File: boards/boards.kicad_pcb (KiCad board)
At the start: 2 copper layers, 34 parts, among them J1 MicroSD, P1 CONN_01X04, P10 , P11 , P12 , P13 CONN_01X02, P2 , P3 , P4 , P5 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

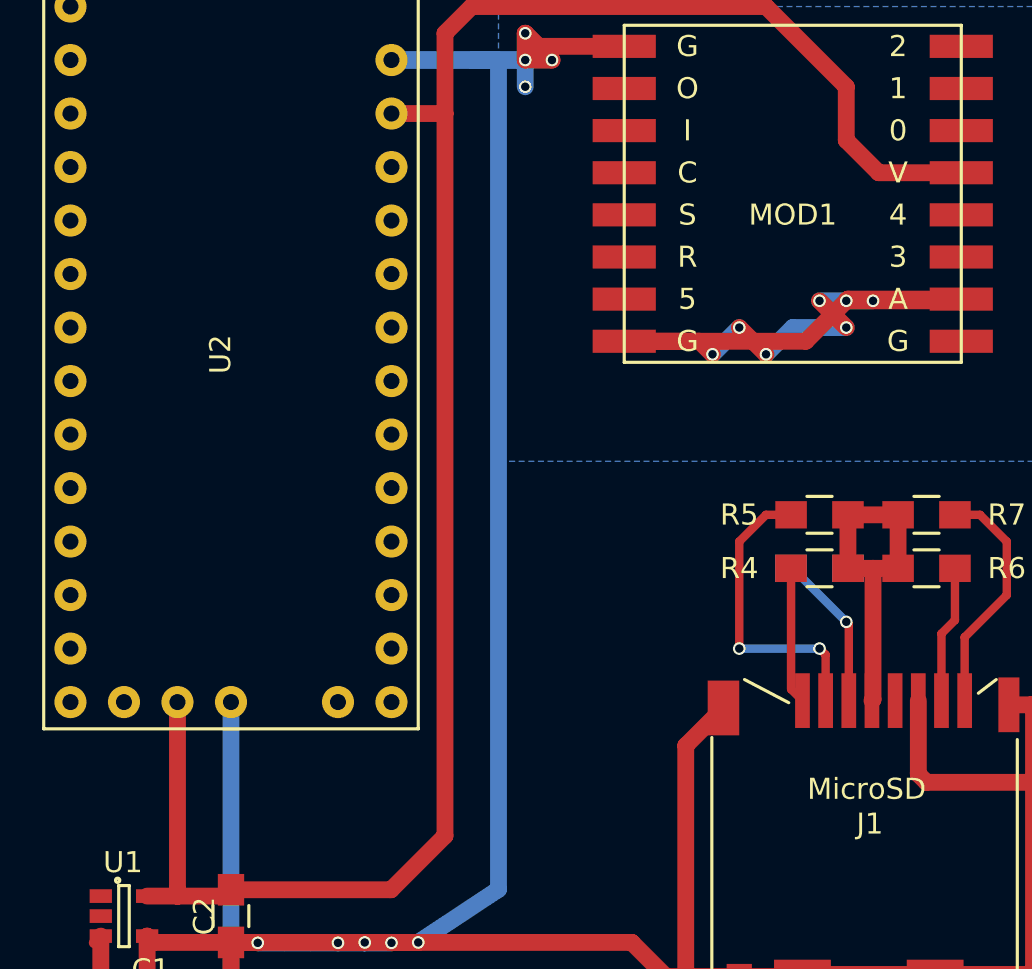
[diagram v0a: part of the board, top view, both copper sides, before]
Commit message: Continued routing SPI pins. Added some relevant offline docs.
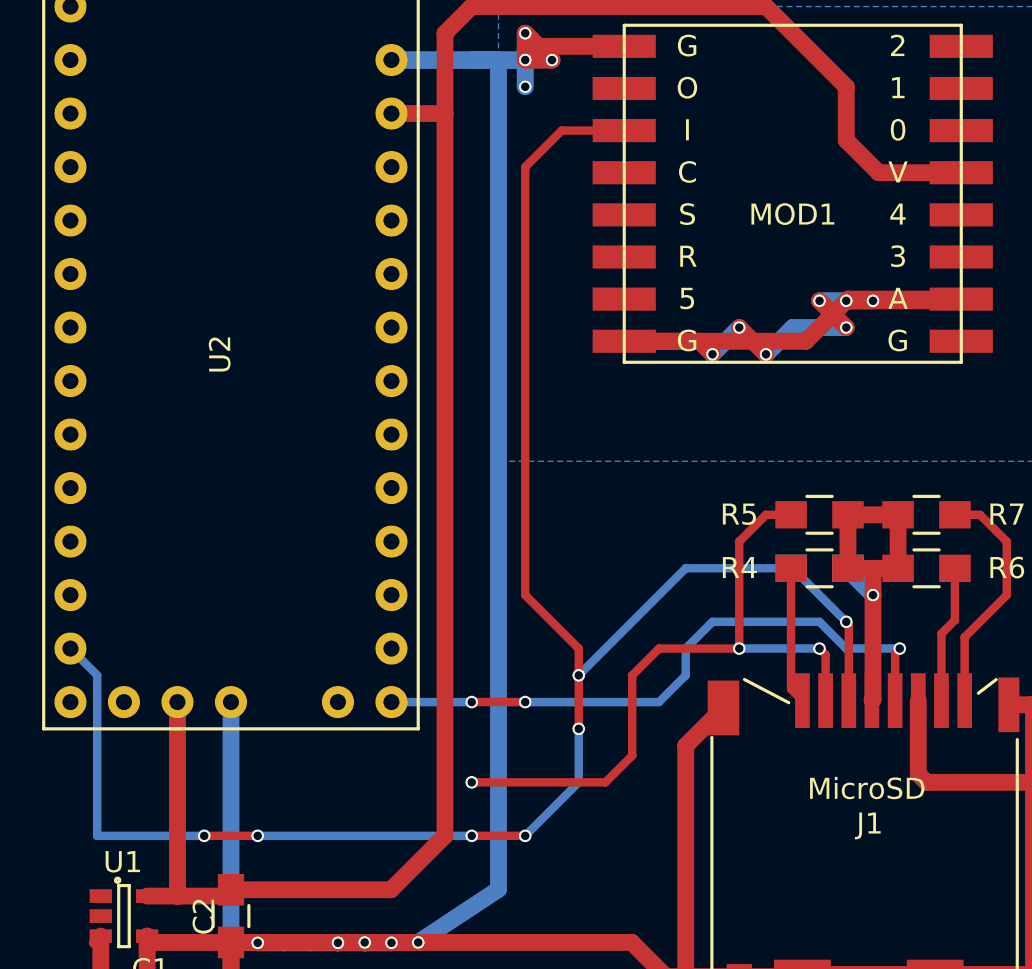
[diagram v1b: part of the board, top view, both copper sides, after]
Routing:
- net Net-(J1-Pad3): track 7.46 -> 88.7 mm, vias 1 -> 7
- net Net-(J1-Pad5): track 0.00 -> 29.5 mm, vias 0 -> 3
- net Net-(J1-Pad2): track 14.5 -> 32.0 mm, vias 2 -> 3
- net +3V3: track 112.2 -> 113.9 mm, vias 0 -> 1
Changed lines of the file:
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@@
   (general
     (links 77)
-    (no_connects 49)
+    (no_connects 45)
     (area 0 0 0 0)
     (thickness 1.6)
     (drawings 4)
-    (tracks 139)
+    (tracks 186)
     (zones 0)
     (modules 34)
@@
     (pad_to_mask_clearance 0.2)
     (aux_axis_origin 0 0)
-    (visible_elements FFFFF37F)
+    (visible_elements FFFFF77F)
     (pcbplotparams
       (layerselection 0x00030_80000001)
@@
     (add_net "Net-(U2-Pad26)")
     (add_net "Net-(U2-Pad30)")
-    (add_net "Net-(U2-Pad31)")
     (add_net SCL)
     (add_net SDA)
@@
   (via (at 71.12 27.94) (size 0.6) (drill 0.4) (layers F.Cu B.Cu) (net 1))
   (segment (start 57.15 68.56) (end 58.4 68.56) (width 0.8) (layer F.Cu) (net 1))
-  (segment (start 69.85 26.67) (end 64.77 26.67) (width 0.8) (layer B.Cu) (net 1) (status 800000))
+  (segment (start 69.85 26.67) (end 64.77 26.67) (width 0.8) (layer B.Cu) (net 1))
   (segment (start 69.85 66.04) (end 69.85 26.67) (width 0.8) (layer B.Cu) (net 1))
   (segment (start 69.85 66.04) (end 69.85 66.04) (width 0.8) (layer B.Cu) (net 1))
@@
   (segment (start 50.65 68.58) (end 50.97 68.26) (width 0.5) (layer F.Cu) (net 2))
   (segment (start 50.97 70.97) (end 50.82 71.12) (width 0.5) (layer F.Cu) (net 2))
-  (segment (start 87.63 50.8) (end 87.63 57.03) (width 0.8) (layer F.Cu) (net 3))
+  (segment (start 86.44 50.8) (end 86.44 50.88) (width 0.8) (layer B.Cu) (net 3) (status C00000))
+  (segment (start 86.44 50.88) (end 87.63 52.07) (width 0.8) (layer B.Cu) (net 3) (status 400000))
+  (via (at 87.63 52.07) (size 0.6) (drill 0.4) (layers F.Cu B.Cu) (net 3))
+  (segment (start 87.63 50.8) (end 87.63 52.07) (width 0.8) (layer F.Cu) (net 3))
+  (segment (start 87.63 52.07) (end 87.63 57.03) (width 0.8) (layer F.Cu) (net 3))
   (segment (start 87.63 57.03) (end 87.58 57.08) (width 0.8) (layer F.Cu) (net 3))
   (segment (start 86.44 48.26) (end 88.82 48.26) (width 0.8) (layer F.Cu) (net 3))
@@
   (segment (start 56.85 66.36) (end 57.15 66.06) (width 0.8) (layer F.Cu) (net 3))
   (segment (start 56.85 66.36) (end 57.15 66.06) (width 0.5) (layer F.Cu) (net 3))
-  (segment (start 83.74 50.8) (end 83.74 56.54) (width 0.4) (layer F.Cu) (net 9) (status 400000))
-  (segment (start 83.74 56.54) (end 84.28 57.08) (width 0.4) (layer F.Cu) (net 9) (status 800000))
-  (segment (start 83.74 48.26) (end 82.55 48.26) (width 0.4) (layer F.Cu) (net 10) (status 400000))
+  (segment (start 83.74 50.8) (end 83.74 56.54) (width 0.4) (layer F.Cu) (net 9))
+  (segment (start 83.74 56.54) (end 84.28 57.08) (width 0.4) (layer F.Cu) (net 9))
+  (via (at 68.58 60.96) (size 0.6) (drill 0.4) (layers F.Cu B.Cu) (net 10))
+  (segment (start 68.58 60.96) (end 74.93 60.96) (width 0.4) (layer F.Cu) (net 10))
+  (segment (start 74.93 60.96) (end 76.2 59.69) (width 0.4) (layer F.Cu) (net 10))
+  (segment (start 76.2 59.69) (end 76.2 55.88) (width 0.4) (layer F.Cu) (net 10))
+  (segment (start 76.2 55.88) (end 77.47 54.61) (width 0.4) (layer F.Cu) (net 10))
+  (segment (start 81.28 54.61) (end 77.47 54.61) (width 0.4) (layer F.Cu) (net 10))
+  (segment (start 83.74 48.26) (end 82.55 48.26) (width 0.4) (layer F.Cu) (net 10))
   (segment (start 82.55 48.26) (end 81.28 49.53) (width 0.4) (layer F.Cu) (net 10))
   (segment (start 81.28 49.53) (end 81.28 54.61) (width 0.4) (layer F.Cu) (net 10))
@@
   (via (at 85.09 54.61) (size 0.6) (drill 0.4) (layers F.Cu B.Cu) (net 10))
   (segment (start 85.09 54.61) (end 85.38 54.9) (width 0.4) (layer F.Cu) (net 10))
-  (segment (start 85.38 54.9) (end 85.38 57.08) (width 0.4) (layer F.Cu) (net 10) (status 800000))
-  (segment (start 83.74 50.8) (end 83.82 50.8) (width 0.25) (layer B.Cu) (net 11) (status C00000))
-  (segment (start 83.82 50.8) (end 86.36 53.34) (width 0.4) (layer B.Cu) (net 11) (status 400000))
-  (segment (start 86.48 53.46) (end 86.48 57.08) (width 0.4) (layer F.Cu) (net 11) (status 800000))
+  (segment (start 85.38 54.9) (end 85.38 57.08) (width 0.4) (layer F.Cu) (net 10))
+  (segment (start 73.66 55.88) (end 73.66 54.61) (width 0.4) (layer F.Cu) (net 11))
+  (segment (start 72.85 30.02) (end 75.82 30.02) (width 0.4) (layer F.Cu) (net 11) (status 800000))
+  (segment (start 71.12 31.75) (end 72.85 30.02) (width 0.4) (layer F.Cu) (net 11))
+  (segment (start 71.12 52.07) (end 71.12 31.75) (width 0.4) (layer F.Cu) (net 11))
+  (segment (start 73.66 54.61) (end 71.12 52.07) (width 0.4) (layer F.Cu) (net 11))
+  (segment (start 49.53 54.61) (end 50.8 55.88) (width 0.4) (layer B.Cu) (net 11) (status 400000))
+  (segment (start 78.74 50.8) (end 83.74 50.8) (width 0.4) (layer B.Cu) (net 11) (status 800000))
+  (segment (start 73.66 55.88) (end 78.74 50.8) (width 0.4) (layer B.Cu) (net 11))
+  (via (at 73.66 55.88) (size 0.6) (drill 0.4) (layers F.Cu B.Cu) (net 11))
+  (segment (start 73.66 58.42) (end 73.66 55.88) (width 0.4) (layer F.Cu) (net 11))
+  (via (at 73.66 58.42) (size 0.6) (drill 0.4) (layers F.Cu B.Cu) (net 11))
+  (segment (start 73.66 60.96) (end 73.66 58.42) (width 0.4) (layer B.Cu) (net 11))
+  (segment (start 71.12 63.5) (end 73.66 60.96) (width 0.4) (layer B.Cu) (net 11))
+  (via (at 71.12 63.5) (size 0.6) (drill 0.4) (layers F.Cu B.Cu) (net 11))
+  (segment (start 68.58 63.5) (end 71.12 63.5) (width 0.4) (layer F.Cu) (net 11))
+  (via (at 68.58 63.5) (size 0.6) (drill 0.4) (layers F.Cu B.Cu) (net 11))
+  (segment (start 58.42 63.5) (end 68.58 63.5) (width 0.4) (layer B.Cu) (net 11))
+  (via (at 58.42 63.5) (size 0.6) (drill 0.4) (layers F.Cu B.Cu) (net 11))
+  (segment (start 55.88 63.5) (end 58.42 63.5) (width 0.4) (layer F.Cu) (net 11))
+  (via (at 55.88 63.5) (size 0.6) (drill 0.4) (layers F.Cu B.Cu) (net 11))
+  (segment (start 50.8 63.5) (end 55.88 63.5) (width 0.4) (layer B.Cu) (net 11))
+  (segment (start 50.8 55.88) (end 50.8 63.5) (width 0.4) (layer B.Cu) (net 11))
+  (segment (start 83.74 50.8) (end 83.82 50.8) (width 0.25) (layer B.Cu) (net 11))
+  (segment (start 83.82 50.8) (end 86.36 53.34) (width 0.4) (layer B.Cu) (net 11))
+  (segment (start 86.48 53.46) (end 86.48 57.08) (width 0.4) (layer F.Cu) (net 11))
   (segment (start 86.36 53.34) (end 86.48 53.46) (width 0.4) (layer F.Cu) (net 11))
   (via (at 86.36 53.34) (size 0.6) (drill 0.4) (layers F.Cu B.Cu) (net 11))
-  (segment (start 91.52 50.8) (end 91.52 53.26) (width 0.4) (layer F.Cu) (net 13) (status 400000))
+  (segment (start 71.12 57.15) (end 77.47 57.15) (width 0.4) (layer B.Cu) (net 12))
+  (segment (start 88.68 54.83) (end 88.9 54.61) (width 0.4) (layer F.Cu) (net 12))
+  (via (at 88.9 54.61) (size 0.6) (drill 0.4) (layers F.Cu B.Cu) (net 12))
+  (segment (start 88.9 54.61) (end 86.36 54.61) (width 0.4) (layer B.Cu) (net 12))
+  (segment (start 86.36 54.61) (end 85.09 53.34) (width 0.4) (layer B.Cu) (net 12))
+  (via (at 71.12 57.15) (size 0.6) (drill 0.4) (layers F.Cu B.Cu) (net 12))
+  (segment (start 71.12 57.15) (end 68.58 57.15) (width 0.4) (layer F.Cu) (net 12))
+  (via (at 68.58 57.15) (size 0.6) (drill 0.4) (layers F.Cu B.Cu) (net 12))
+  (segment (start 64.77 57.15) (end 68.58 57.15) (width 0.4) (layer B.Cu) (net 12))
+  (segment (start 88.68 54.83) (end 88.68 57.08) (width 0.4) (layer F.Cu) (net 12))
+  (segment (start 81.28 53.34) (end 85.09 53.34) (width 0.4) (layer B.Cu) (net 12))
+  (segment (start 80.01 53.34) (end 81.28 53.34) (width 0.4) (layer B.Cu) (net 12))
+  (segment (start 78.74 54.61) (end 80.01 53.34) (width 0.4) (layer B.Cu) (net 12))
+  (segment (start 78.74 55.88) (end 78.74 54.61) (width 0.4) (layer B.Cu) (net 12))
+  (segment (start 77.47 57.15) (end 78.74 55.88) (width 0.4) (layer B.Cu) (net 12))
+  (segment (start 91.52 50.8) (end 91.52 53.26) (width 0.4) (layer F.Cu) (net 13))
   (segment (start 91.52 53.26) (end 90.88 53.9) (width 0.4) (layer F.Cu) (net 13))
-  (segment (start 90.88 53.9) (end 90.88 57.08) (width 0.4) (layer F.Cu) (net 13) (status 800000))
-  (segment (start 91.52 48.26) (end 92.71 48.26) (width 0.4) (layer F.Cu) (net 14) (status 400000))
-  (segment (start 91.98 54.07) (end 91.98 57.08) (width 0.4) (layer F.Cu) (net 14) (status 800000))
+  (segment (start 90.88 53.9) (end 90.88 57.08) (width 0.4) (layer F.Cu) (net 13))
+  (segment (start 91.52 48.26) (end 92.71 48.26) (width 0.4) (layer F.Cu) (net 14))
+  (segment (start 91.98 54.07) (end 91.98 57.08) (width 0.4) (layer F.Cu) (net 14))
   (segment (start 93.98 52.07) (end 91.98 54.07) (width 0.4) (layer F.Cu) (net 14))
   (segment (start 93.98 49.53) (end 93.98 52.07) (width 0.4) (layer F.Cu) (net 14))
